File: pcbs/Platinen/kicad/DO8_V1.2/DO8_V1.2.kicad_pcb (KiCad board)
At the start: 4 copper layers, 100 x 77 mm, 115 parts, among them IC1 ITS4880R, J1 Conn_01x04, J10 TBL009-500-02GY-2GY, J11 TBL009-500-02GY-2GY, J2 Conn_01x02, J3 Conn_01x02, J4 Conn_02x03_Odd_Even, J5 Conn_02x05_Odd_Even, J6 Conn_02x05_Odd_Even, J7 TBL009-500-02GY-2GY, J8 TBL009-500-02GY-2GY, J9 TBL009-500-02GY-2GY, Q1 BC846, Q2 BC846, Q3 BC846, Q4 BC846, Q5 BC846, Q6 BC846, Q7 BC846, Q8 BC846, Q9 FQP27P06, SW1 SW_DIP_x05, U1 SN65HVD232, U2 MAX485E, U3 STM32F103C8Tx, U4 AP1117-33, U5 TLP291-4, U6 TLP291-4, U7 TLP291-4, U8 TLP291-4, Y1 8MHz

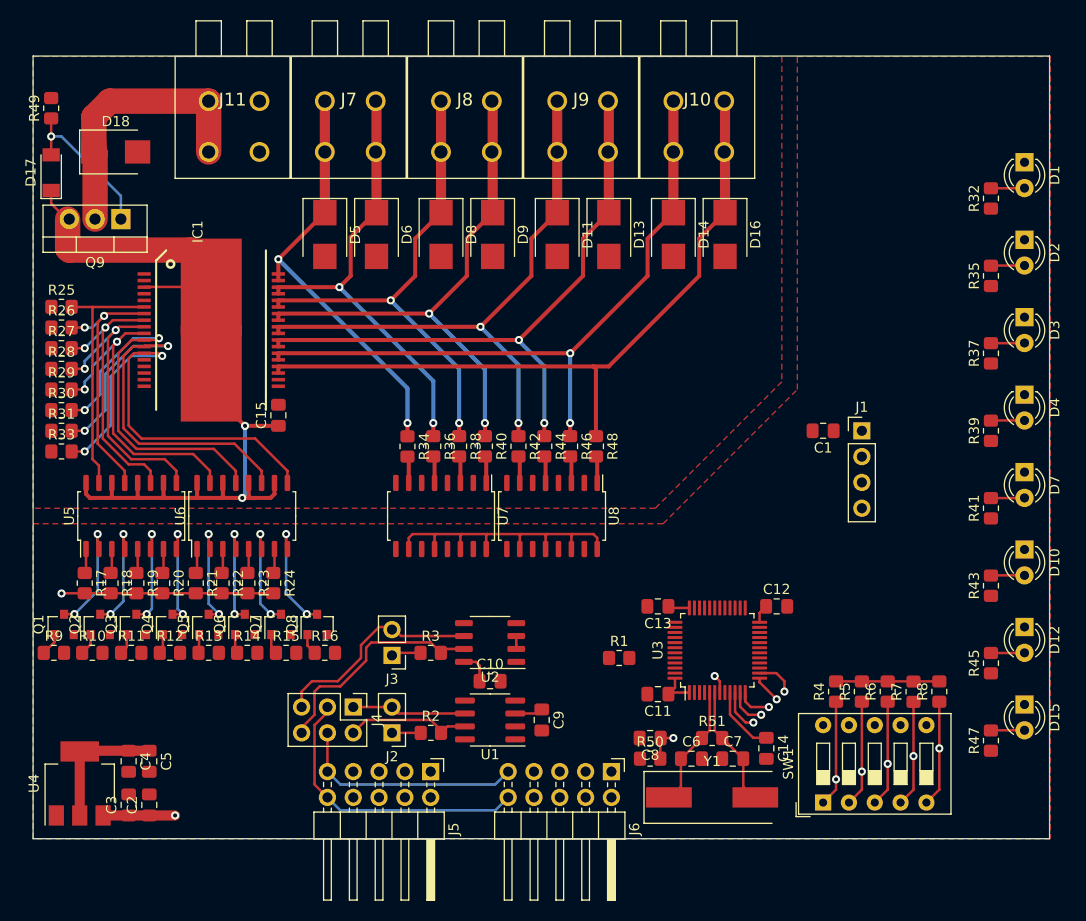
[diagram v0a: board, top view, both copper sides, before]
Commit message: finalizing DO8_V1.2 Routing
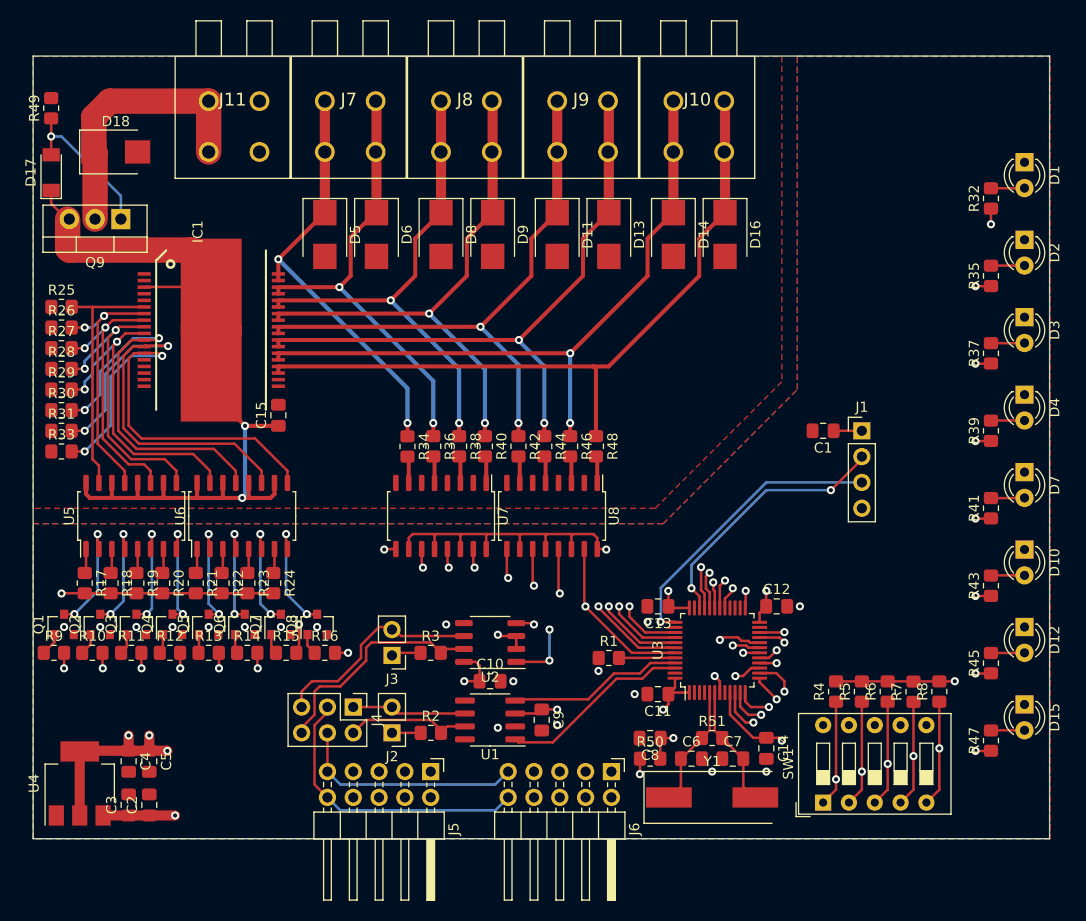
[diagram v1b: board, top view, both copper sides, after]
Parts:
- moved R1 1.02 mm to (126.9, 132.2)
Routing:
- net FB1: track 0.00 -> 116.8 mm, vias 0 -> 3
- net FB2: track 0.00 -> 107.0 mm, vias 0 -> 3
- net FB3: track 0.00 -> 99.4 mm, vias 0 -> 3
- net FB4: track 0.00 -> 89.2 mm, vias 0 -> 3
- net FB8: track 0.00 -> 77.8 mm, vias 0 -> 2
- net FB7: track 0.00 -> 75.1 mm, vias 0 -> 3
- net CH1: track 0.00 -> 72.9 mm, vias 0 -> 2
- net FB6: track 0.00 -> 72.9 mm, vias 0 -> 3
- net FB5: track 0.00 -> 72.6 mm, vias 0 -> 3
- net CH2: track 0.00 -> 72.2 mm, vias 0 -> 2
- net CH3: track 0.00 -> 69.7 mm, vias 0 -> 2
- net CH4: track 0.00 -> 65.0 mm, vias 0 -> 2
- net CH5: track 0.00 -> 61.4 mm, vias 0 -> 2
- net CH7: track 0.00 -> 56.3 mm, vias 0 -> 2
- net CH6: track 0.00 -> 56.2 mm, vias 0 -> 2
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- added copper zone on B.Cu, net +3V3

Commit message: finalize DO8 layout
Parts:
- added G***: LOGO, KiCAD_personal:logo_new, F.Cu at (155.3, 80.4)
- added REF**: OSHW-Logo2_9.8x8mm_SilkScreen, Symbol:OSHW-Logo2_9.8x8mm_SilkScreen, F.Cu at (155.3, 101.2)
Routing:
- net GND2: vias 0 -> 52
- net GND: vias 18 -> 65
- added copper zone on In1.Cu, net GND
- added copper zone on In2.Cu, net GND
- added copper zone on B.Cu, net GND2
- added copper zone on In1.Cu, net GND2
- added copper zone on In2.Cu, net GND2
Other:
- board text added: "Marco Müller not revved by theBrutzler yet"
- board text added: "SynPLC DO8 V1.2 21.06.21"

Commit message: finished layouts
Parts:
- added D19: LL4148, Diode_SMD:D_MiniMELF, F.Cu at (107.1, 106.8)
- added D20: LL4148, Diode_SMD:D_MiniMELF, F.Cu at (109.6, 106.8)
- added D21: LL4148, Diode_SMD:D_MiniMELF, F.Cu at (112.2, 106.8)
- added D22: LL4148, Diode_SMD:D_MiniMELF, F.Cu at (114.7, 106.8)
- added D23: LL4148, Diode_SMD:D_MiniMELF, F.Cu at (118.0, 106.8)
- added D24: LL4148, Diode_SMD:D_MiniMELF, F.Cu at (120.5, 106.8)
- added D25: LL4148, Diode_SMD:D_MiniMELF, F.Cu at (123.1, 106.8)
- added D26: LL4148, Diode_SMD:D_MiniMELF, F.Cu at (125.6, 106.8)
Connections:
- D5 pad 1: Net-(D5-Pad1) -> Net-(D19-Pad2)
- D6 pad 1: Net-(D6-Pad1) -> Net-(D20-Pad2)
- D8 pad 1: Net-(D8-Pad1) -> Net-(D21-Pad2)
- D9 pad 1: Net-(D9-Pad1) -> Net-(D22-Pad2)
- IC1 pad 29: Net-(D9-Pad1) -> Net-(D22-Pad2)
- IC1 pad 30: Net-(D9-Pad1) -> Net-(D22-Pad2)
- IC1 pad 31: Net-(D8-Pad1) -> Net-(D21-Pad2)
- IC1 pad 32: Net-(D8-Pad1) -> Net-(D21-Pad2)
- IC1 pad 33: Net-(D6-Pad1) -> Net-(D20-Pad2)
- IC1 pad 34: Net-(D6-Pad1) -> Net-(D20-Pad2)
- IC1 pad 35: Net-(D5-Pad1) -> Net-(D19-Pad2)
- IC1 pad 36: Net-(D5-Pad1) -> Net-(D19-Pad2)
- J7 pad 1: Net-(D5-Pad1) -> Net-(D19-Pad2)
- J7 pad 2: Net-(D5-Pad1) -> Net-(D19-Pad2)
- J7 pad 3: Net-(D6-Pad1) -> Net-(D20-Pad2)
- J7 pad 4: Net-(D6-Pad1) -> Net-(D20-Pad2)
- J8 pad 1: Net-(D8-Pad1) -> Net-(D21-Pad2)
- J8 pad 2: Net-(D8-Pad1) -> Net-(D21-Pad2)
- J8 pad 3: Net-(D9-Pad1) -> Net-(D22-Pad2)
- J8 pad 4: Net-(D9-Pad1) -> Net-(D22-Pad2)
- R34 pad 1: Net-(D5-Pad1) -> Net-(D19-Pad1)
- R36 pad 1: Net-(D6-Pad1) -> Net-(D20-Pad1)
- R38 pad 1: Net-(D8-Pad1) -> Net-(D21-Pad1)
- R40 pad 1: Net-(D9-Pad1) -> Net-(D22-Pad1)
- R42 pad 1: Net-(D11-Pad1) -> Net-(D23-Pad1)
- R44 pad 1: Net-(D13-Pad1) -> Net-(D24-Pad1)
- R46 pad 1: Net-(D14-Pad1) -> Net-(D25-Pad1)
- R48 pad 1: Net-(D16-Pad1) -> Net-(D26-Pad1)
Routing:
- net Net-(D9-Pad1): track 53.3 -> 0.00 mm, vias 2 -> 0
- net Net-(D22-Pad2): track 0.00 -> 51.0 mm, vias 0 -> 2
- net Net-(D8-Pad1): track 49.5 -> 0.00 mm, vias 2 -> 0
- net Net-(D21-Pad2): track 0.00 -> 47.2 mm, vias 0 -> 2
- net Net-(D6-Pad1): track 45.1 -> 0.00 mm, vias 2 -> 0
- net Net-(D20-Pad2): track 0.00 -> 42.7 mm, vias 0 -> 2
- net Net-(D5-Pad1): track 42.2 -> 0.00 mm, vias 2 -> 0
- net Net-(D19-Pad2): track 0.00 -> 39.9 mm, vias 0 -> 2
- net Net-(D16-Pad1): track 71.0 -> 65.7 mm
- net Net-(D14-Pad1): track 66.5 -> 64.2 mm
- net Net-(D13-Pad1): track 62.0 -> 59.7 mm
- net Net-(D11-Pad1): track 58.2 -> 55.8 mm
- net Net-(D26-Pad1): track 0.00 -> 1.82 mm
- net Net-(D19-Pad1): track 0.00 -> 1.30 mm
- net Net-(D25-Pad1): track 0.00 -> 1.29 mm
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
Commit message: started revs
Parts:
- moved C15 21.3 mm to (79.0, 93.6), turned to 270 degrees
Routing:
- net Net-(IC1-Pad12): track 43.5 -> 33.0 mm
- net Net-(IC1-Pad13): track 44.5 -> 35.1 mm
- net Net-(IC1-Pad11): track 39.5 -> 31.0 mm
- net +24V: track 85.6 -> 82.2 mm
- net Net-(D19-Pad2): track 39.9 -> 41.9 mm
- net DIR: track 31.6 -> 33.4 mm
- net Net-(D20-Pad2): track 42.7 -> 43.7 mm
- net Net-(D14-Pad1): track 64.2 -> 65.1 mm
- net Net-(D21-Pad2): track 47.2 -> 48.1 mm
- net Net-(D13-Pad1): track 59.7 -> 60.5 mm
- net Net-(D11-Pad1): track 55.8 -> 56.7 mm
- net Net-(D22-Pad2): track 51.0 -> 51.9 mm
- net Net-(D16-Pad1): track 65.7 -> 66.5 mm
- net RXD: track 32.3 -> 31.4 mm, vias 3 -> 2
- net CH7: track 56.3 -> 55.5 mm
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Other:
- board text added: "Marco Müller revved by Blind_Via"
- board text removed: "Marco Müller not revved by theBrutzler yet"

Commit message: complete reviews from dave
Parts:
- added REF**: ESD-Logo_6.6x6mm_SilkScreen, Symbol:ESD-Logo_6.6x6mm_SilkScreen, F.Cu at (158.5, 100.5)
- moved REF** 3.81 mm to (151.5, 101.2)
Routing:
- net FB8: track 77.8 -> 73.3 mm
- net FB7: track 75.1 -> 70.6 mm
- net FB6: track 72.9 -> 68.5 mm
- net CH8: track 47.6 -> 45.5 mm
- net SWIO: track 25.9 -> 26.8 mm
- net GND2: vias 54 -> 59
